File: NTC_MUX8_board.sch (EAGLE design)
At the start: 58 parts, among them IC1 NINA-B306-00B, IC2 INA126E, IC3 MCP6001T_SOT23, IC4 MAX8559ETAAA+T, J1 USB4105-GF-A, J2 1761681-7, J3 DM3CS-SF-PEJMS, J4 DNP, Q1 NTR5103NT1G, Q2 NTR5103NT1G, T1N TESTPOINT_TPS-SMD-10SN, T1P TESTPOINT_TPS-SMD-10SN, U1 TMUX1208PWR, U2 TMUX1208PWR, U3 TMUX1208PWR, U4 TMUX1208PWR

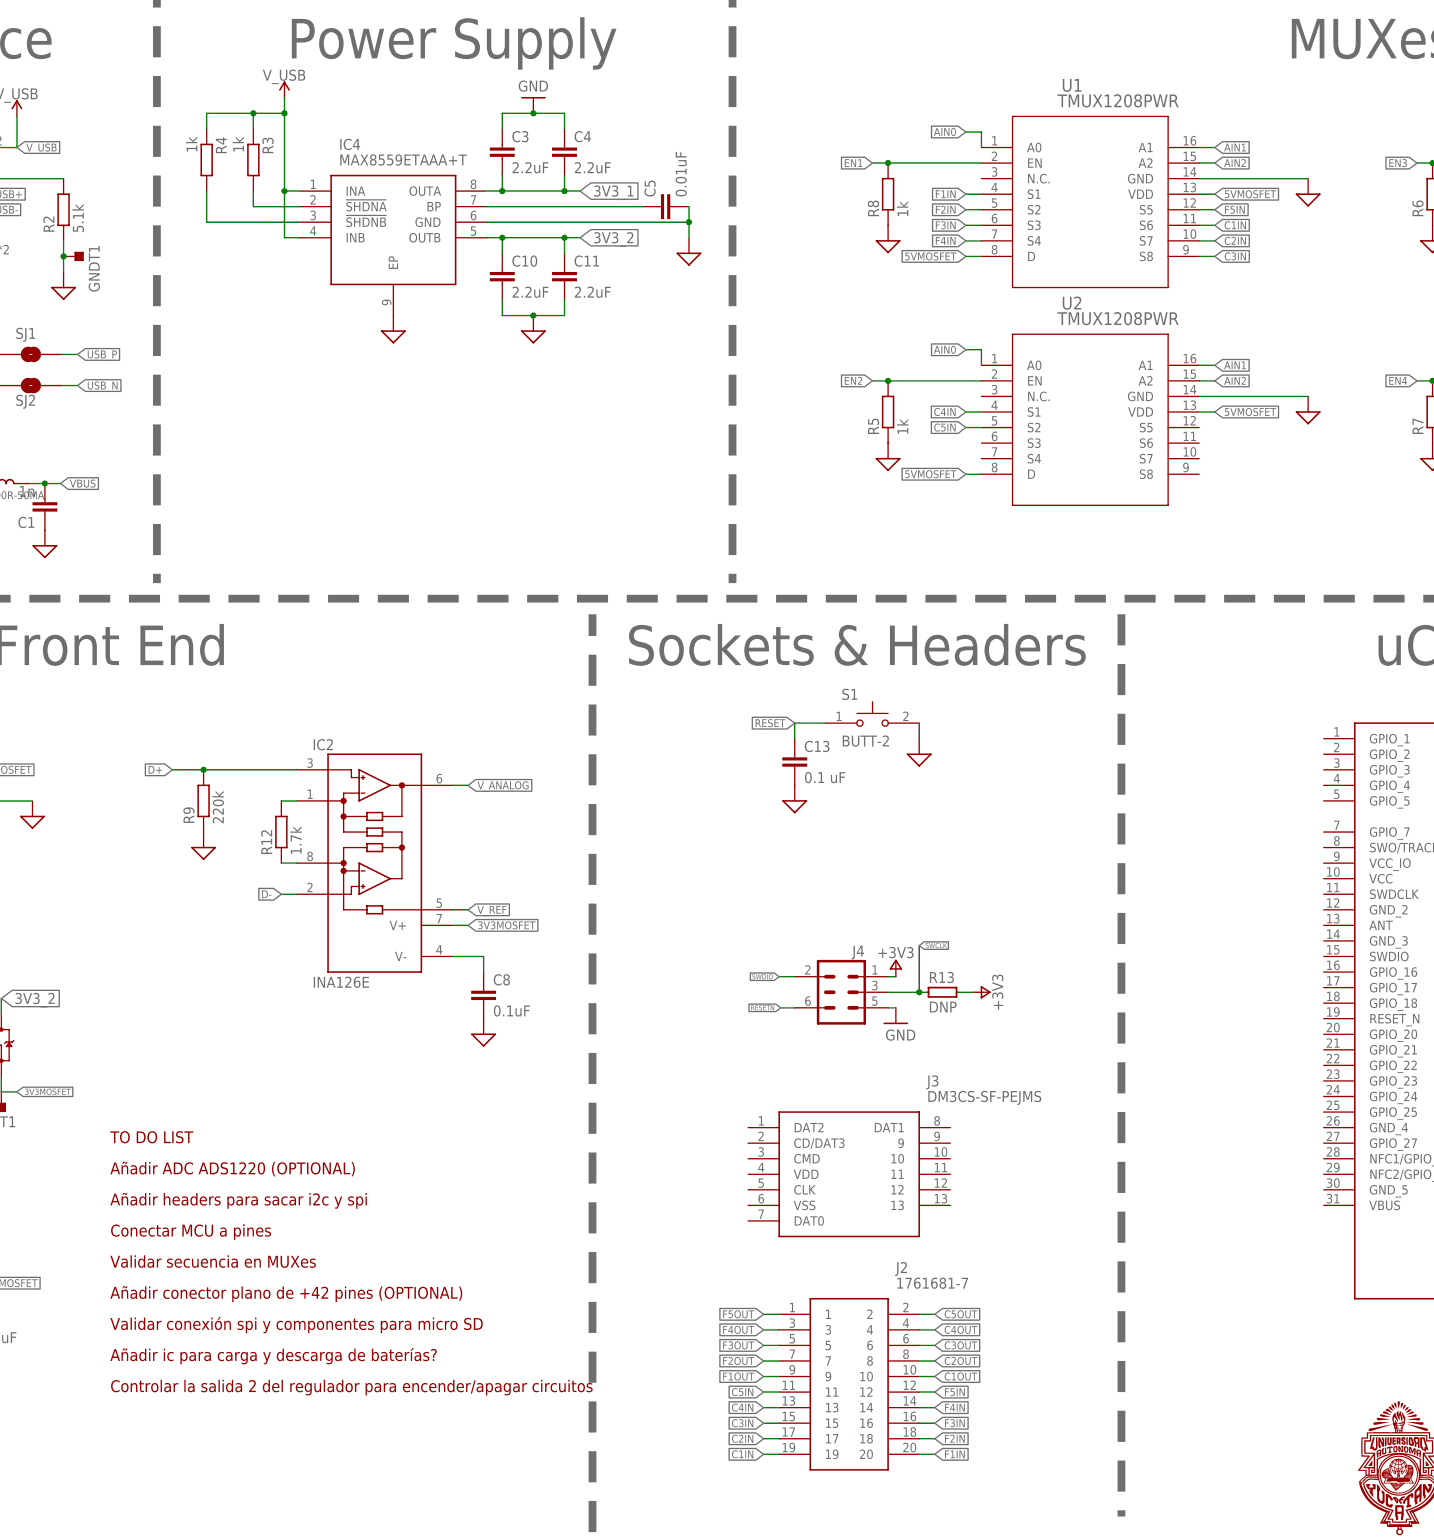
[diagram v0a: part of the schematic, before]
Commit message: 3d models updated
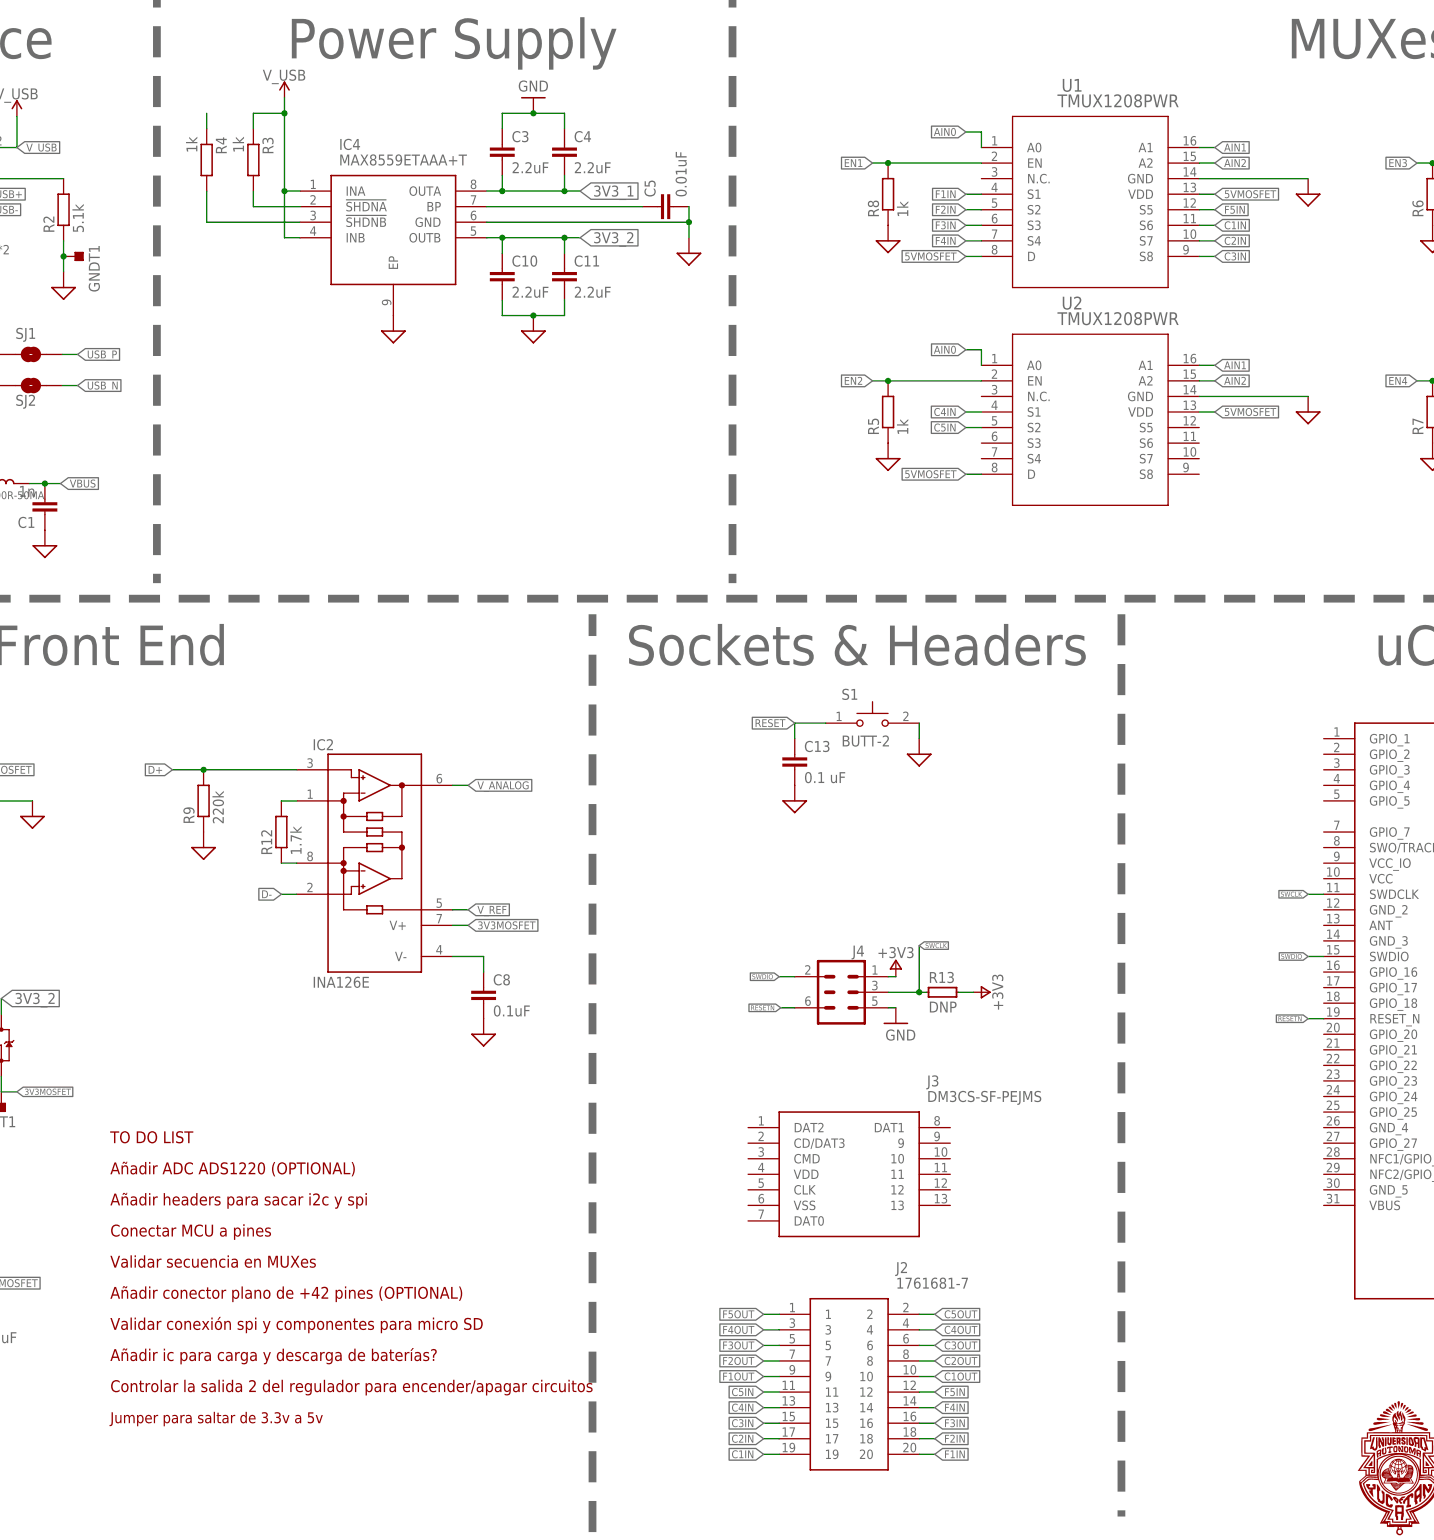
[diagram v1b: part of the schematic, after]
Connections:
- new net N$10: R4.1
- net RESETN: now also IC1.RESET_N
- net SWCLK: now also IC1.SWDCLK
- net SWDIO: now also IC1.SWDIO
- net V_USB: no longer R4.1
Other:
- note added: "Jumper para saltar de 3.3v a 5v"

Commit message: detalles
faltan los detalles marcados en el esquemático
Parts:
- removed 3V3T1, GNDT1, T1N, T1P: TESTPOINT_TPS-SMD-10SN, 52101-101-REV-A_v16:TESTPOINT_TPS-SMD-10SN
- removed C6, C7: 1n, rcl:C-EUC0603
- removed FB1: FERRITE_BEAD, Filter:FBCHIP-0603(1608-METRIC)
- removed FID4: FIDUCIAL_1MM, microbuilder:FIDUCIAL_1MM
- removed Q2: NTR5103NT1G, NTR5103NT1G:NTR5103NT1G
- added 3V3T2: TESTPOINT_TPS-SMD-10SN, 52101-101-REV-A_v16:TESTPOINT_TPS-SMD-10SN
- added D2: SML-P12PTT86R, SML-P12PTT86R:SML-P12PTT86R
- added J5: (no value), con-lstb:MA04-2
- added J6: (no value), con-lstb:MA06-2
- added JP1: JUMPER-SMT_3_NO_NO-SILK, SparkFun-Jumpers:JUMPER-SMT_3_NO_NO-SILK
- added R14: DNP, rcl:R-EU_R0603
- added R15: 1k, rcl:R-EU_R0603
- added R16, R17: 4k7, rcl:R-EU_R0603
- added R18, R19, R20, R21: 10k, rcl:R-EU_R0603
- IC1: value NINA-B306-00B -> NINA-B306-00B-00; device NINA-B306-00B:NINA-B306-00B -> NINA-B306-00B-00:NINA-B306-00B-00
- R13: device Arduino-rcl:R-DNP-0402 -> rcl:R-EU_R0603
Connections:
- removed net +3V3: J4.1, R13.1
- removed net 3V3MOSFET: 3V3T1.TP, C9.1, IC2.V+, IC3.VDD, Q2.S, R10.1
- removed net CS_U: RV1.~CS
- removed net MOSFET2: Q2.G
- removed net N$10: R4.1
- removed net SCK_U: RV1.SCK
- removed net SI_U: RV1.SI
- removed net SWCLK: IC1.SWDCLK, J4.3, R13.2
- removed net V_MIC: C7.2, FB1.2
- new net CS_3: IC1.GPIO_4, J6.4
- new net CS_4: IC1.GPIO_5, J6.3
- new net DP_CS: IC1.GPIO_2, RV1.~CS
- new net GP_PB: JP1.3
- new net I2C_SCL: IC1.GPIO_18, J5.1, J5.2, R16.2
- new net I2C_SDA: IC1.GPIO_20, J5.3, J5.4, R17.2
- new net N$13: R21.1
- new net PWR_LED: IC1.TRACE_D3/GPIO_33, R15.2
- new net R_PULLUP: IC1.SWO/TRACE_D0/GPIO_8, R16.1, R17.1
- new net SD_CS: IC1.GPIO_3, J3.CD/DAT3
- new net SPI_MISO: IC1.GPIO_34, J3.DAT0, J6.5, J6.6, R18.1
- new net SPI_MOSI: IC1.GPIO_35, J3.CMD, J6.7, J6.8, R19.1, RV1.SI
- new net SPI_SCK: IC1.GPIO_1, J3.CLK, J6.10, J6.9, R20.1, RV1.SCK
- new net SWDCLK: IC1.SWDCLK, J4.3, R14.2
- new net V_EN: IC1.QSPI_D2/GPIO_49, IC4.!SHDNB, R4.2
- net 3V3_1: now also IC1.VCC, IC1.VCC_IO, J4.1, R13.2, R14.1, R4.1
- net 3V3_2: now also 3V3T2.TP, C9.1, IC2.V+, IC3.VDD, J3.VDD, J5.7, J5.8, J6.11, J6.12, R10.1, R18.2, R19.2, R20.2, R21.2; no longer Q2.D
- net EN1: now also IC1.GPIO_24
- net EN2: now also IC1.GPIO_23
- net EN3: now also IC1.GPIO_21
- net EN4: now also IC1.GPIO_22
- net GND: now also D2.K, IC1.EGP, IC1.GND, J3.10, J3.11, J3.12, J3.13, J3.9, J3.VSS, J5.5, J5.6, J6.1, J6.2; no longer C6.1, C7.1, GNDT1.TP
- net N$3: now also D2.A, R15.1; no longer IC4.!SHDNB, R4.2
- net RESET: now also JP1.2, R13.1
- net RESETN: now also IC1.!RESET, JP1.1; no longer IC1.RESET_N
- net USB+: no longer T1P.TP
- net USB-: no longer T1N.TP
- net USB_N: now also IC1.USB_DM
- net USB_P: now also IC1.USB_DP
- net VBUS: now also IC1.VBUS, Q1.D
- net V_ANALOG: now also IC1.GPIO_25
- net V_USB: no longer C6.2, FB1.1, Q1.D
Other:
- note added: "Añadir ADC ADS1220 (FUTURO)"
- note added: "Añadir conector plano de +42 pines (FUTURO)"
- note added: "Añadir ic para carga y descarga de baterías (FUTURO)"
- note added: "NTC MUX Board Rev1.5"
- note added: "Revisar mosfets, se están usando como canal P y no N"
- note added: "editar footprint de nina para quitar todos los gpio no usados"
- note removed: "Añadir ADC ADS1220 (OPTIONAL)"
- note removed: "Añadir conector plano de +42 pines (OPTIONAL)"
- note removed: "Añadir ic para carga y descarga de baterías?"
- note removed: "NTC MUX Board Rev1.4"
- note removed: "SOLO VA UNO?"
- moved on the sheet: C1, C13, C2, D1, J2, J3, L1, R4, S1, SJ1, SJ2

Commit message: Pequeños errores y adición de mejoras
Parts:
- removed 5VMT1: TESTPOINT_TPS-SMD-10SN, 52101-101-REV-A_v16:TESTPOINT_TPS-SMD-10SN
- removed Q1: NTR5103NT1G, NTR5103NT1G:NTR5103NT1G
- added J7: 52808-2071, 52808-2071:52808-2071
- added SV1: (no value), con-lstb:MA03-1
- added TPSV+: TESTPOINT_TPS-SMD-10SN, 52101-101-REV-A_v16:TESTPOINT_TPS-SMD-10SN
- added X1: 22-23-2021, con-molex:22-23-2021
- renumbered 3V3T2 to 3V3T1
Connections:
- net EN1 renamed ENI1
- net EN2 renamed ENI2
- removed net 5VMOSFET: 5VMT1.TP, C12.1, Q1.S, RV1.PA0, RV1.VDD, U1.D, U1.VDD, U2.D, U2.VDD, U3.VDD, U4.VDD
- removed net EN3: IC1.GPIO_21, R6.2, U3.EN
- removed net EN4: IC1.GPIO_22, R7.2, U4.EN
- removed net MOSFET1: Q1.G
- removed net N$13: R21.1
- new net DAT: J3.DAT1, J3.DAT2, R21.1
- new net ENO1: IC1.GPIO_22, R6.2, U3.EN
- new net ENO2: IC1.GPIO_21, R7.2, U4.EN
- new net VSEL: C12.1, RV1.PA0, RV1.VDD, SV1.2, TPSV+.TP, U1.D, U1.VDD, U2.D, U2.VDD, U3.VDD, U4.VDD
- net 3V3_1: now also 3V3T1.TP
- net 3V3_2: now also SV1.3; no longer 3V3T1.TP
- net AIN0: now also IC1.QSPI_D2/GPIO_49
- net AIN1: now also IC1.GPIO_27
- net AIN2: now also IC1.GPIO_44
- net AOUT0: now also IC1.GPIO_39
- net AOUT1: now also IC1.GPIO_41
- net AOUT2: now also IC1.GPIO_43
- net C1IN: now also J2.20, J7.20, U2.S1; no longer J2.19, U1.S6
- net C1OUT: now also J2.9, J7.9, U4.S1; no longer J2.10, U3.S6
- net C2IN: now also J2.18, J7.18, U2.S2; no longer J2.17, U1.S7
- net C2OUT: now also J2.7, J7.7, U4.S2; no longer J2.8, U3.S7
- net C3IN: now also J2.16, J7.16, U2.S3; no longer J2.15, U1.S8
- net C3OUT: now also J2.5, J7.5, U4.S3; no longer J2.6, U3.S8
- net C4IN: now also J2.14, J7.14, U2.S4; no longer J2.13, U2.S1
- net C4OUT: now also J2.3, J7.3, U4.S4; no longer J2.4, U4.S1
- net C5IN: now also J2.12, J7.12, U2.S5; no longer J2.11, U2.S2
- net C5OUT: now also J2.1, J7.1, U4.S5; no longer J2.2, U4.S2
- net CS_3: now also J6.3; no longer J6.4
- net CS_4: now also J6.4; no longer J6.3
- net F1IN: now also J2.19, J7.19; no longer J2.20
- net F1OUT: now also J2.10, J7.10; no longer J2.9
- net F2IN: now also J2.17, J7.17; no longer J2.18
- net F2OUT: now also J2.8, J7.8; no longer J2.7
- net F3IN: now also J2.15, J7.15; no longer J2.16
- net F3OUT: now also J2.6, J7.6; no longer J2.5
- net F4IN: now also J2.13, J7.13; no longer J2.14
- net F4OUT: now also J2.4, J7.4; no longer J2.3
- net F5IN: now also J2.11, J7.11; no longer J2.12
- net F5OUT: now also J2.2, J7.2; no longer J2.1
- net GND: now also X1-1.S
- net GP_PB: now also IC1.GPIO_37
- net VBUS: no longer Q1.D
- net V_EN: now also IC1.QSPI_D0/GPIO_50; no longer IC1.QSPI_D2/GPIO_49
- net V_USB: now also SV1.1, X1-2.S
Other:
- note removed: "Añadir ADC ADS1220 (FUTURO)"
- note removed: "Añadir conector plano de +42 pines (FUTURO)"
- note removed: "Añadir headers para sacar i2c y spi"
- note removed: "Añadir ic para carga y descarga de baterías (FUTURO)"
- note removed: "Conectar MCU a pines"
- note removed: "Controlar la salida 2 del regulador para encender/apagar circuitos"
- note removed: "Jumper para saltar de 3.3v a 5v"
- note removed: "Revisar mosfets, se están usando como canal P y no N"
- note removed: "TO DO LIST"
- note removed: "Validar conexión spi y componentes para micro SD"
- note removed: "Validar secuencia en MUXes"
- note removed: "editar footprint de nina para quitar todos los gpio no usados"
- moved on the sheet: C12, C13, C8, C9, IC2, IC3, J2, J3, J4, J5, J6, JP1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
